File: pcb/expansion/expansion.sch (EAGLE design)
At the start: 53 parts, among them IC3 STM32F042F4, J1 AUDIO_JACK_3.5MM_PTH, J2 AUDIO_JACK_3.5MM_PTH, J3 AUDIO_JACK_3.5MM_PTH, J4 AUDIO_JACK_3.5MM_PTH, J5 AUDIO_JACK_3.5MM_PTH, J6 AUDIO_JACK_3.5MM_PTH, SW3 324_SW, SW4 324_SW, U1 USBC_16P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

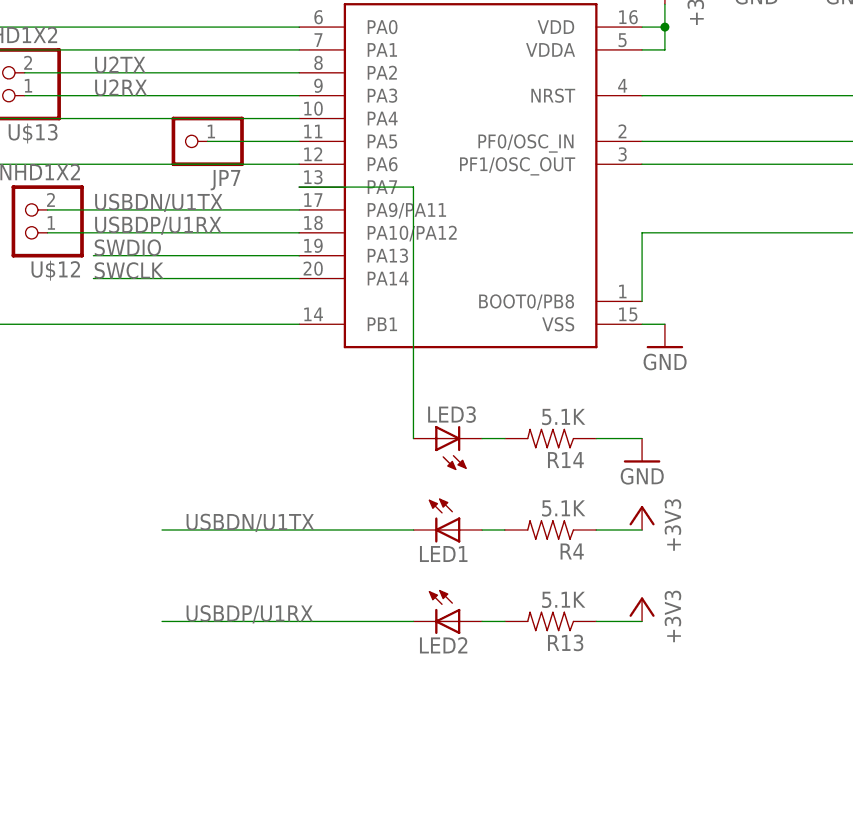
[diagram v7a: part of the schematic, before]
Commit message: removed leds
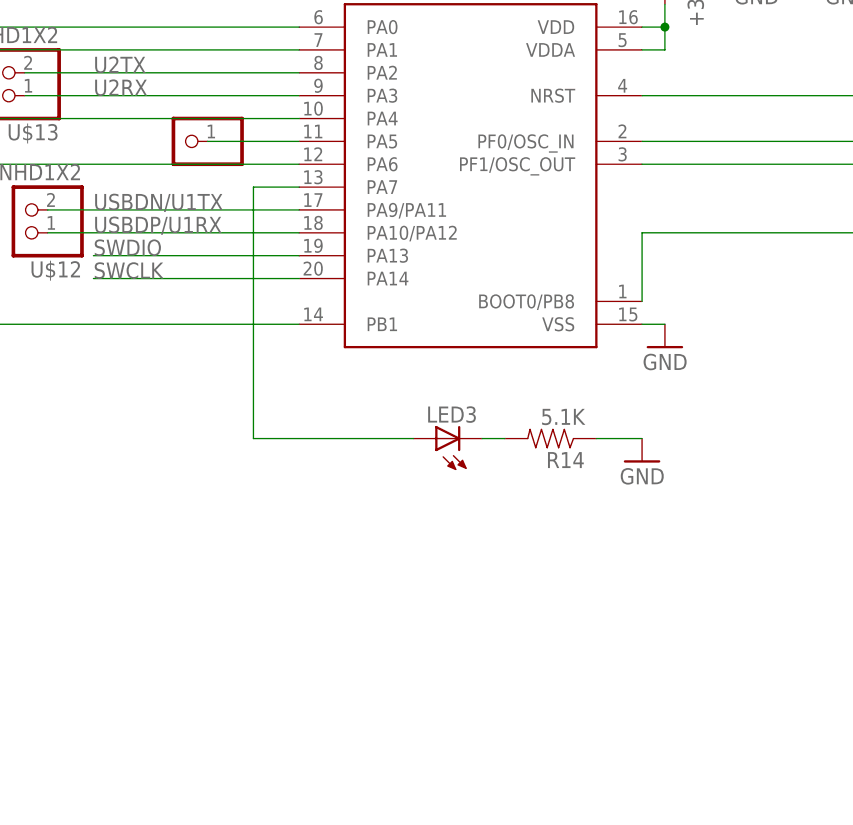
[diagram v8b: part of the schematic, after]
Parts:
- removed LED1, LED2: (no value), adafruit:LEDCHIP-LED0805
- removed R13, R4: 5.1K, SparkFun-Passives:RESISTOR0805-RES
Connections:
- removed net N$10: LED2.A, R13.2
- removed net N$5: LED1.A, R4.2
- net +3V3: no longer R13.1, R4.1
- net USBDN/U1TX: no longer LED1.C
- net USBDP/U1RX: no longer LED2.C
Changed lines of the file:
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@@
 <part name="SW3" library="3pos_slide_switch_centered" deviceset="324_SW" device="" value="324_SW"/>
 <part name="SW4" library="3pos_slide_switch_centered" deviceset="324_SW" device="" value="324_SW"/>
-<part name="LED1" library="adafruit" deviceset="LED" device="CHIP-LED0805"/>
-<part name="R4" library="SparkFun-Passives" deviceset="RESISTOR" device="0805-RES" value="5.1K"/>
 <part name="R5" library="joyAnalog" deviceset="RESISTOR" device="0805-RES" value="10K"/>
 <part name="GND10" library="supply1" deviceset="GND" device=""/>
@@
 <part name="GND25" library="supply1" deviceset="GND" device=""/>
 <part name="GND26" library="supply1" deviceset="GND" device=""/>
-<part name="LED2" library="adafruit" deviceset="LED" device="CHIP-LED0805"/>
-<part name="R13" library="SparkFun-Passives" deviceset="RESISTOR" device="0805-RES" value="5.1K"/>
-<part name="+3V13" library="supply1" library_urn="urn:adsk.eagle:library:371" deviceset="+3V3" device=""/>
-<part name="+3V14" library="supply1" library_urn="urn:adsk.eagle:library:371" deviceset="+3V3" device=""/>
 <part name="U$12" library="adafruit_changed" deviceset="PINHD1X2" device=""/>
 <part name="U$13" library="adafruit_changed" deviceset="PINHD1X2" device=""/>
@@
 <instance part="SW3" gate="G$1" x="91.44" y="55.88" smashed="yes" rot="R90"/>
 <instance part="SW4" gate="G$1" x="91.44" y="2.54" smashed="yes" rot="MR270"/>
-<instance part="LED1" gate="G$1" x="0" y="-15.24" smashed="yes" rot="R270">
-<attribute name="NAME" x="-4.572" y="-18.796" size="1.778" layer="95"/>
-<attribute name="VALUE" x="-4.572" y="-20.955" size="1.778" layer="96"/>
-</instance>
-<instance part="R4" gate="G$1" x="10.16" y="-15.24" smashed="yes" rot="R180">
-<attribute name="NAME" x="13.97" y="-16.7386" size="1.778" layer="95" rot="R180"/>
-<attribute name="VALUE" x="13.97" y="-11.938" size="1.778" layer="96" rot="R180"/>
-</instance>
 <instance part="R5" gate="G$1" x="76.2" y="12.7" smashed="yes" rot="MR90">
 <attribute name="NAME" x="77.6986" y="8.89" size="1.778" layer="95" rot="MR90"/>
@@
 <attribute name="VALUE" x="-35.56" y="-134.62" size="1.778" layer="96" rot="MR0"/>
 </instance>
-<instance part="LED2" gate="G$1" x="0" y="-25.4" smashed="yes" rot="R270">
-<attribute name="NAME" x="-4.572" y="-28.956" size="1.778" layer="95"/>
-<attribute name="VALUE" x="-4.572" y="-31.115" size="1.778" layer="96"/>
-</instance>
-<instance part="R13" gate="G$1" x="10.16" y="-25.4" smashed="yes" rot="R180">
-<attribute name="NAME" x="13.97" y="-26.8986" size="1.778" layer="95" rot="R180"/>
-<attribute name="VALUE" x="13.97" y="-22.098" size="1.778" layer="96" rot="R180"/>
-</instance>
-<instance part="+3V13" gate="G$1" x="20.32" y="-12.7" smashed="yes" rot="MR0">
-<attribute name="VALUE" x="22.86" y="-17.78" size="1.778" layer="96" rot="MR90"/>
-</instance>
-<instance part="+3V14" gate="G$1" x="20.32" y="-22.86" smashed="yes" rot="MR0">
-<attribute name="VALUE" x="22.86" y="-27.94" size="1.778" layer="96" rot="MR90"/>
-</instance>
 <instance part="U$12" gate="1" x="-48.26" y="20.32" smashed="yes" rot="R180">
 <attribute name="NAME" x="-41.91" y="14.605" size="1.778" layer="95" rot="R180"/>
@@
 </instance>
 <instance part="JP7" gate="G$1" x="-30.48" y="27.94" smashed="yes" rot="R180">
-<attribute name="NAME" x="-24.13" y="24.765" size="1.778" layer="95" rot="R180"/>
 <attribute name="VALUE" x="-24.13" y="33.02" size="1.778" layer="96" rot="R180"/>
 </instance>
@@
 <junction x="93.98" y="17.78"/>
 </segment>
-<segment>
-<pinref part="+3V14" gate="G$1" pin="+3V3"/>
-<pinref part="R13" gate="G$1" pin="1"/>
-<wire x1="20.32" y1="-25.4" x2="15.24" y2="-25.4" width="0.1524" layer="91"/>
-</segment>
-<segment>
-<pinref part="+3V13" gate="G$1" pin="+3V3"/>
-<pinref part="R4" gate="G$1" pin="1"/>
-<wire x1="20.32" y1="-15.24" x2="15.24" y2="-15.24" width="0.1524" layer="91"/>
-</segment>
 </net>
 <net name="USBDP/U1RX" class="0">
@@
 <pinref part="U$12" gate="1" pin="1"/>
 </segment>
-<segment>
-<wire x1="-5.08" y1="-25.4" x2="-33.02" y2="-25.4" width="0.1524" layer="91"/>
-<label x="-30.48" y="-25.4" size="1.778" layer="95"/>
-<pinref part="LED2" gate="G$1" pin="C"/>
-</segment>
 </net>
 <net name="N$31" class="0">
@@
 <label x="-40.64" y="20.32" size="1.778" layer="95"/>
 <pinref part="U$12" gate="1" pin="2"/>
-</segment>
-<segment>
-<wire x1="-33.02" y1="-15.24" x2="-5.08" y2="-15.24" width="0.1524" layer="91"/>
-<label x="-30.48" y="-15.24" size="1.778" layer="95"/>
-<pinref part="LED1" gate="G$1" pin="C"/>
 </segment>
 </net>
@@
 </segment>
 </net>
-<net name="N$5" class="0">
-<segment>
-<pinref part="R4" gate="G$1" pin="2"/>
-<pinref part="LED1" gate="G$1" pin="A"/>
-<wire x1="5.08" y1="-15.24" x2="2.54" y2="-15.24" width="0.1524" layer="91"/>
-</segment>
-</net>
-<net name="N$10" class="0">
-<segment>
-<pinref part="R13" gate="G$1" pin="2"/>
-<pinref part="LED2" gate="G$1" pin="A"/>
-<wire x1="5.08" y1="-25.4" x2="2.54" y2="-25.4" width="0.1524" layer="91"/>
-</segment>
-</net>
 <net name="N$11" class="0">
 <segment>
@@
 <pinref part="IC3" gate="G$1" pin="PA7"/>
 <pinref part="LED3" gate="G$1" pin="A"/>
-<wire x1="-17.78" y1="22.86" x2="-5.08" y2="22.86" width="0.1524" layer="91"/>
-<wire x1="-5.08" y1="22.86" x2="-5.08" y2="-5.08" width="0.1524" layer="91"/>
-</segment>
-</net>
+<wire x1="-17.78" y1="22.86" x2="-22.86" y2="22.86" width="0.1524" layer="91"/>
+<wire x1="-22.86" y1="22.86" x2="-22.86" y2="-5.08" width="0.1524" layer="91"/>
+<wire x1="-22.86" y1="-5.08" x2="-5.08" y2="-5.08" width="0.1524" layer="91"/>
+</segment>
+</net>
